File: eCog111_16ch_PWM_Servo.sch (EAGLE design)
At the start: 1 part

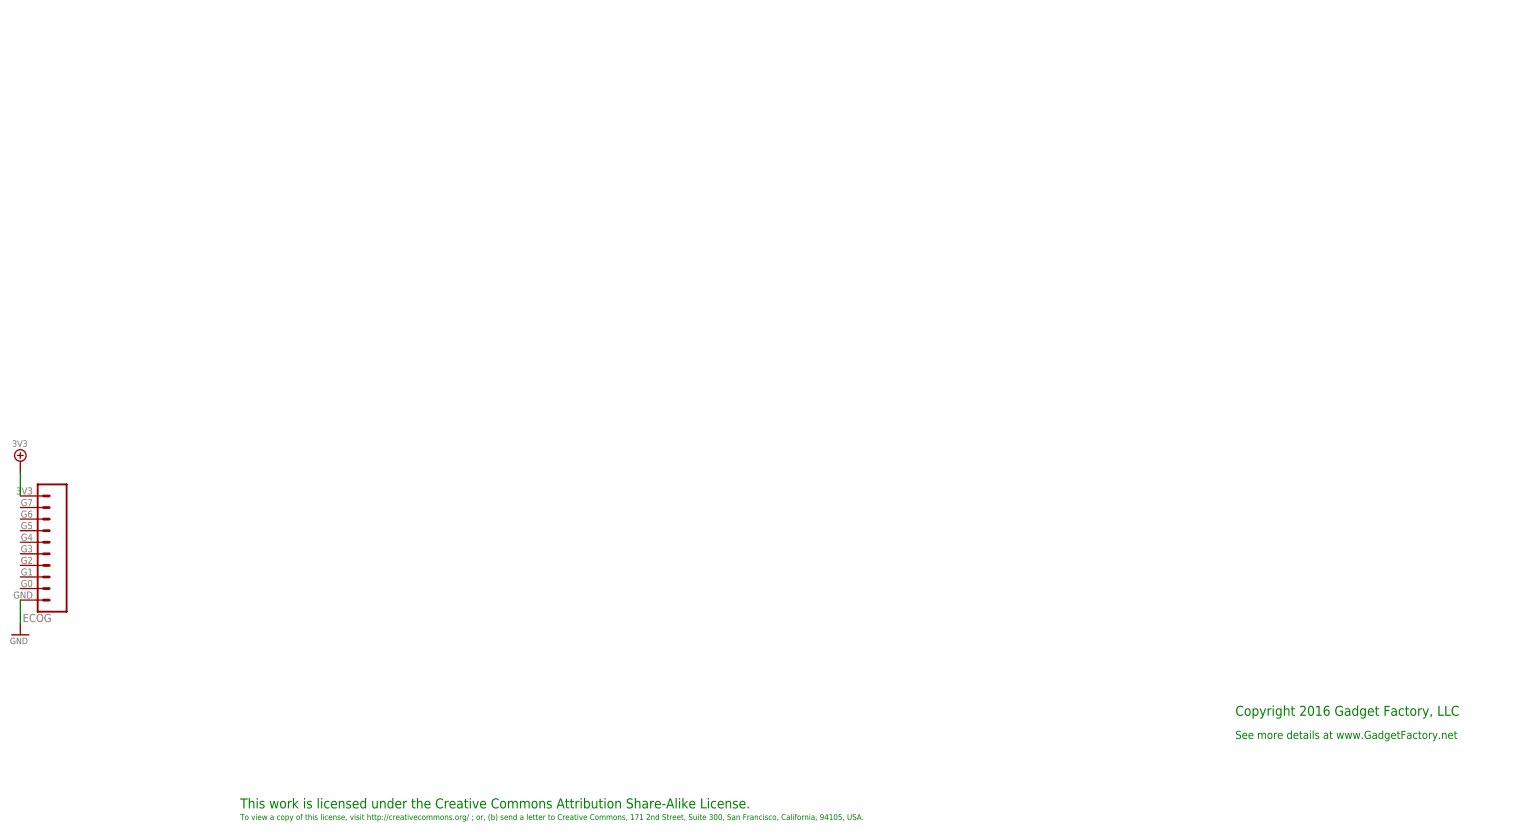
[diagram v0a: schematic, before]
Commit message: Added new eCogs
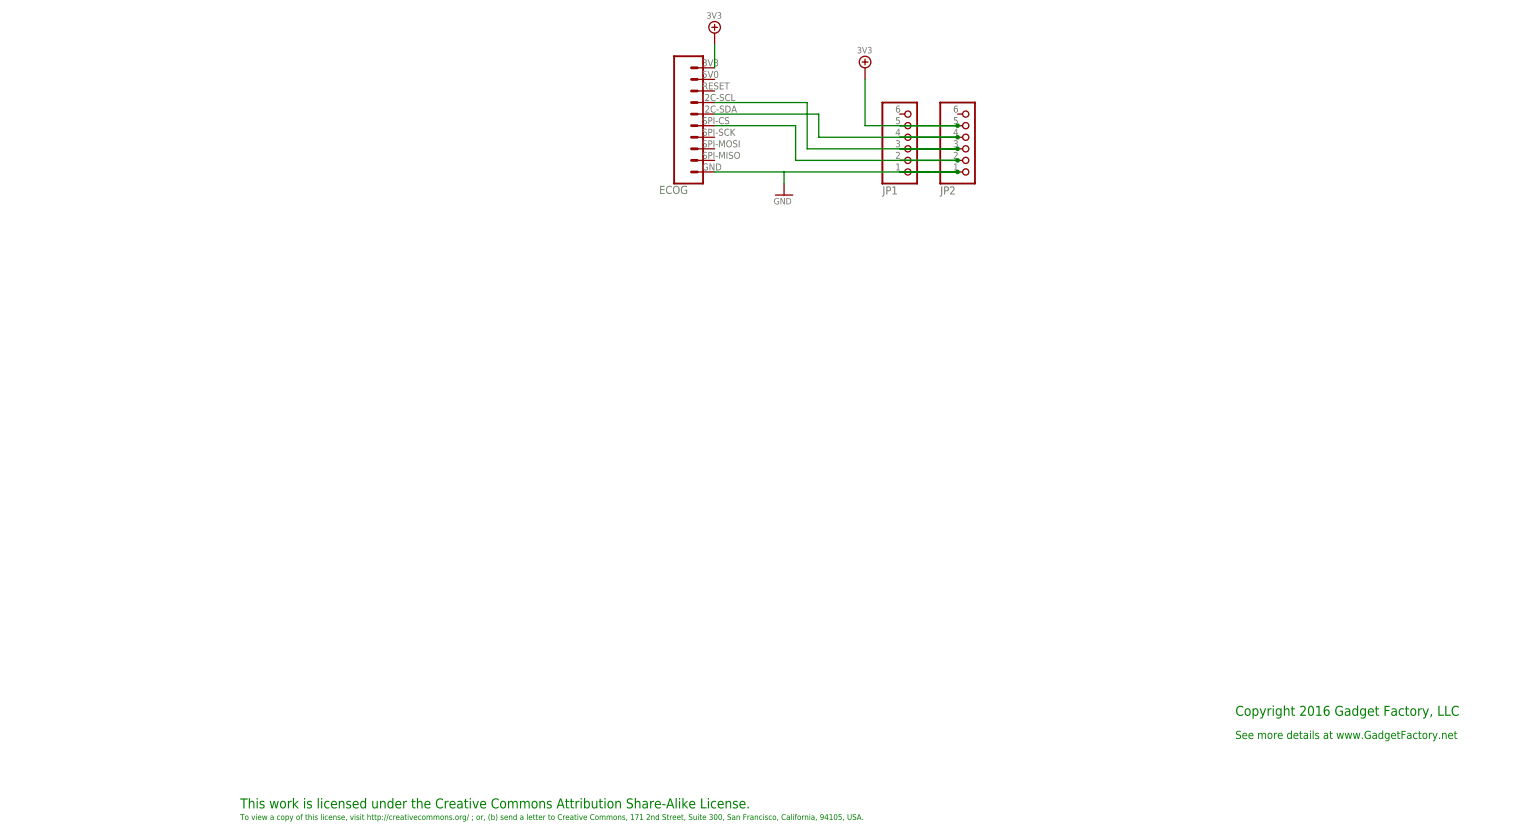
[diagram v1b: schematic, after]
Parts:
- added JP1, JP2: (no value), GadgetFactory:PINHD-1X6
- ECOG: value ECOG_GENERAL_ROWECOG_GENERAL_SMD -> ECOG_BUSES_ROWECOG_BUSES_SMD; device eCogs:ECOG_GENERAL_ROWECOG_GENERAL_SMD -> eCogs:ECOG_BUSES_ROWECOG_BUSES_SMD
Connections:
- new net N$1: ECOG.SPI-CS@B3, JP1.2, JP2.2
- new net N$2: ECOG.I2C-SCL@B5, JP1.3, JP2.3
- new net N$3: ECOG.I2C-SDA@B4, JP1.4, JP2.4
- net 3V3: now also ECOG.3V3@B8, JP1.5, JP2.5; no longer ECOG.3V3
- net GND: now also ECOG.GND@B, JP1.1, JP2.1; no longer ECOG.GND
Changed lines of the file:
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@@
 <parts>
 <part name="FRAME1" library="frames" deviceset="A3L-LOC" device=""/>
-<part name="ECOG" library="eCogs" deviceset="ECOG_GENERAL_ROW" device="ECOG_GENERAL_SMD" value="ECOG_GENERAL_ROWECOG_GENERAL_SMD"/>
+<part name="ECOG" library="eCogs" deviceset="ECOG_BUSES_ROW" device="ECOG_BUSES_SMD" value="ECOG_BUSES_ROWECOG_BUSES_SMD"/>
+<part name="GND1" library="eCogs" deviceset="GND" device=""/>
 <part name="3V3_PWR1" library="eCogs" deviceset="3V3" device=""/>
-<part name="GND1" library="eCogs" deviceset="GND" device=""/>
+<part name="JP1" library="GadgetFactory" deviceset="PINHD-1X6" device=""/>
+<part name="JP2" library="GadgetFactory" deviceset="PINHD-1X6" device=""/>
+<part name="3V3_PWR2" library="eCogs" deviceset="3V3" device=""/>
 </parts>
 <sheets>
@@
 <instances>
 <instance part="FRAME1" gate="G$1" x="0" y="0"/>
-<instance part="ECOG" gate="ECOG_GENERAL" x="55.88" y="53.34"/>
-<instance part="3V3_PWR1" gate="A" x="50.8" y="86.36"/>
-<instance part="GND1" gate="A" x="50.8" y="48.26"/>
+<instance part="ECOG" gate="ECOG_BUSES" x="195.58" y="147.32"/>
+<instance part="GND1" gate="A" x="218.44" y="144.78"/>
+<instance part="3V3_PWR1" gate="A" x="203.2" y="180.34"/>
+<instance part="JP1" gate="A" x="246.38" y="157.48" rot="MR180"/>
+<instance part="JP2" gate="A" x="259.08" y="157.48" rot="MR180"/>
+<instance part="3V3_PWR2" gate="A" x="236.22" y="172.72"/>
 </instances>
 <busses>
 </busses>
 <nets>
+<net name="GND" class="0">
+<segment>
+<pinref part="ECOG" gate="ECOG_BUSES" pin="GND@B"/>
+<pinref part="GND1" gate="A" pin="GND"/>
+<wire x1="203.2" y1="149.86" x2="218.44" y2="149.86" width="0.2032" layer="91"/>
+<wire x1="218.44" y1="149.86" x2="218.44" y2="147.32" width="0.2032" layer="91"/>
+<pinref part="JP1" gate="A" pin="1"/>
+<wire x1="256.54" y1="149.86" x2="218.44" y2="149.86" width="0.2032" layer="91"/>
+<pinref part="JP2" gate="A" pin="1"/>
+<junction x="256.54" y="149.86"/>
+<wire x1="256.54" y1="149.86" x2="243.84" y2="149.86" width="0.1524" layer="91"/>
+</segment>
+</net>
 <net name="3V3" class="0">
 <segment>
-<pinref part="ECOG" gate="ECOG_GENERAL" pin="3V3"/>
 <pinref part="3V3_PWR1" gate="A" pin="3V3"/>
-<wire x1="50.8" y1="83.82" x2="50.8" y2="78.74" width="0.1524" layer="91"/>
+<pinref part="ECOG" gate="ECOG_BUSES" pin="3V3@B8"/>
+<wire x1="203.2" y1="177.8" x2="203.2" y2="172.72" width="0.2032" layer="91"/>
+</segment>
+<segment>
+<pinref part="JP1" gate="A" pin="5"/>
+<pinref part="JP2" gate="A" pin="5"/>
+<wire x1="256.54" y1="160.02" x2="236.22" y2="160.02" width="0.2032" layer="91"/>
+<wire x1="236.22" y1="160.02" x2="236.22" y2="170.18" width="0.2032" layer="91"/>
+<pinref part="3V3_PWR2" gate="A" pin="3V3"/>
+<junction x="256.54" y="160.02"/>
+<wire x1="256.54" y1="160.02" x2="243.84" y2="160.02" width="0.1524" layer="91"/>
 </segment>
 </net>
-<net name="GND" class="0">
+<net name="N$1" class="0">
 <segment>
-<pinref part="ECOG" gate="ECOG_GENERAL" pin="GND"/>
-<pinref part="GND1" gate="A" pin="GND"/>
-<wire x1="50.8" y1="55.88" x2="50.8" y2="50.8" width="0.2032" layer="91"/>
+<pinref part="JP1" gate="A" pin="2"/>
+<pinref part="JP2" gate="A" pin="2"/>
+<wire x1="256.54" y1="152.4" x2="220.98" y2="152.4" width="0.2032" layer="91"/>
+<wire x1="220.98" y1="152.4" x2="220.98" y2="160.02" width="0.2032" layer="91"/>
+<pinref part="ECOG" gate="ECOG_BUSES" pin="SPI-CS@B3"/>
+<wire x1="220.98" y1="160.02" x2="203.2" y2="160.02" width="0.2032" layer="91"/>
+<junction x="256.54" y="152.4"/>
+<wire x1="256.54" y1="152.4" x2="243.84" y2="152.4" width="0.1524" layer="91"/>
 </segment>
 </net>
+<net name="N$2" class="0">
+<segment>
+<pinref part="JP1" gate="A" pin="3"/>
+<pinref part="JP2" gate="A" pin="3"/>
+<wire x1="256.54" y1="154.94" x2="223.52" y2="154.94" width="0.2032" layer="91"/>
+<wire x1="223.52" y1="154.94" x2="223.52" y2="165.1" width="0.2032" layer="91"/>
+<pinref part="ECOG" gate="ECOG_BUSES" pin="I2C-SCL@B5"/>
+<wire x1="223.52" y1="165.1" x2="203.2" y2="165.1" width="0.2032" layer="91"/>
+<junction x="256.54" y="154.94"/>
+<wire x1="256.54" y1="154.94" x2="243.84" y2="154.94" width="0.1524" layer="91"/>
+</segment>
+</net>
+<net name="N$3" class="0">
+<segment>
+<pinref part="JP1" gate="A" pin="4"/>
+<pinref part="JP2" gate="A" pin="4"/>
+<wire x1="256.54" y1="157.48" x2="226.06" y2="157.48" width="0.2032" layer="91"/>
+<wire x1="226.06" y1="157.48" x2="226.06" y2="162.56" width="0.2032" layer="91"/>
+<pinref part="ECOG" gate="ECOG_BUSES" pin="I2C-SDA@B4"/>
+<wire x1="226.06" y1="162.56" x2="203.2" y2="162.56" width="0.2032" layer="91"/>
+<junction x="256.54" y="157.48"/>
+<wire x1="256.54" y1="157.48" x2="243.84" y2="157.48" width="0.1524" layer="91"/>
+</segment>
+</net>
